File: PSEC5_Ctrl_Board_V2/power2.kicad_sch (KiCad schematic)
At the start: 41 parts, among them J1 1766343, U16 OKX-T/5-D12N-C, U5 OKX-T/5-D12N-C

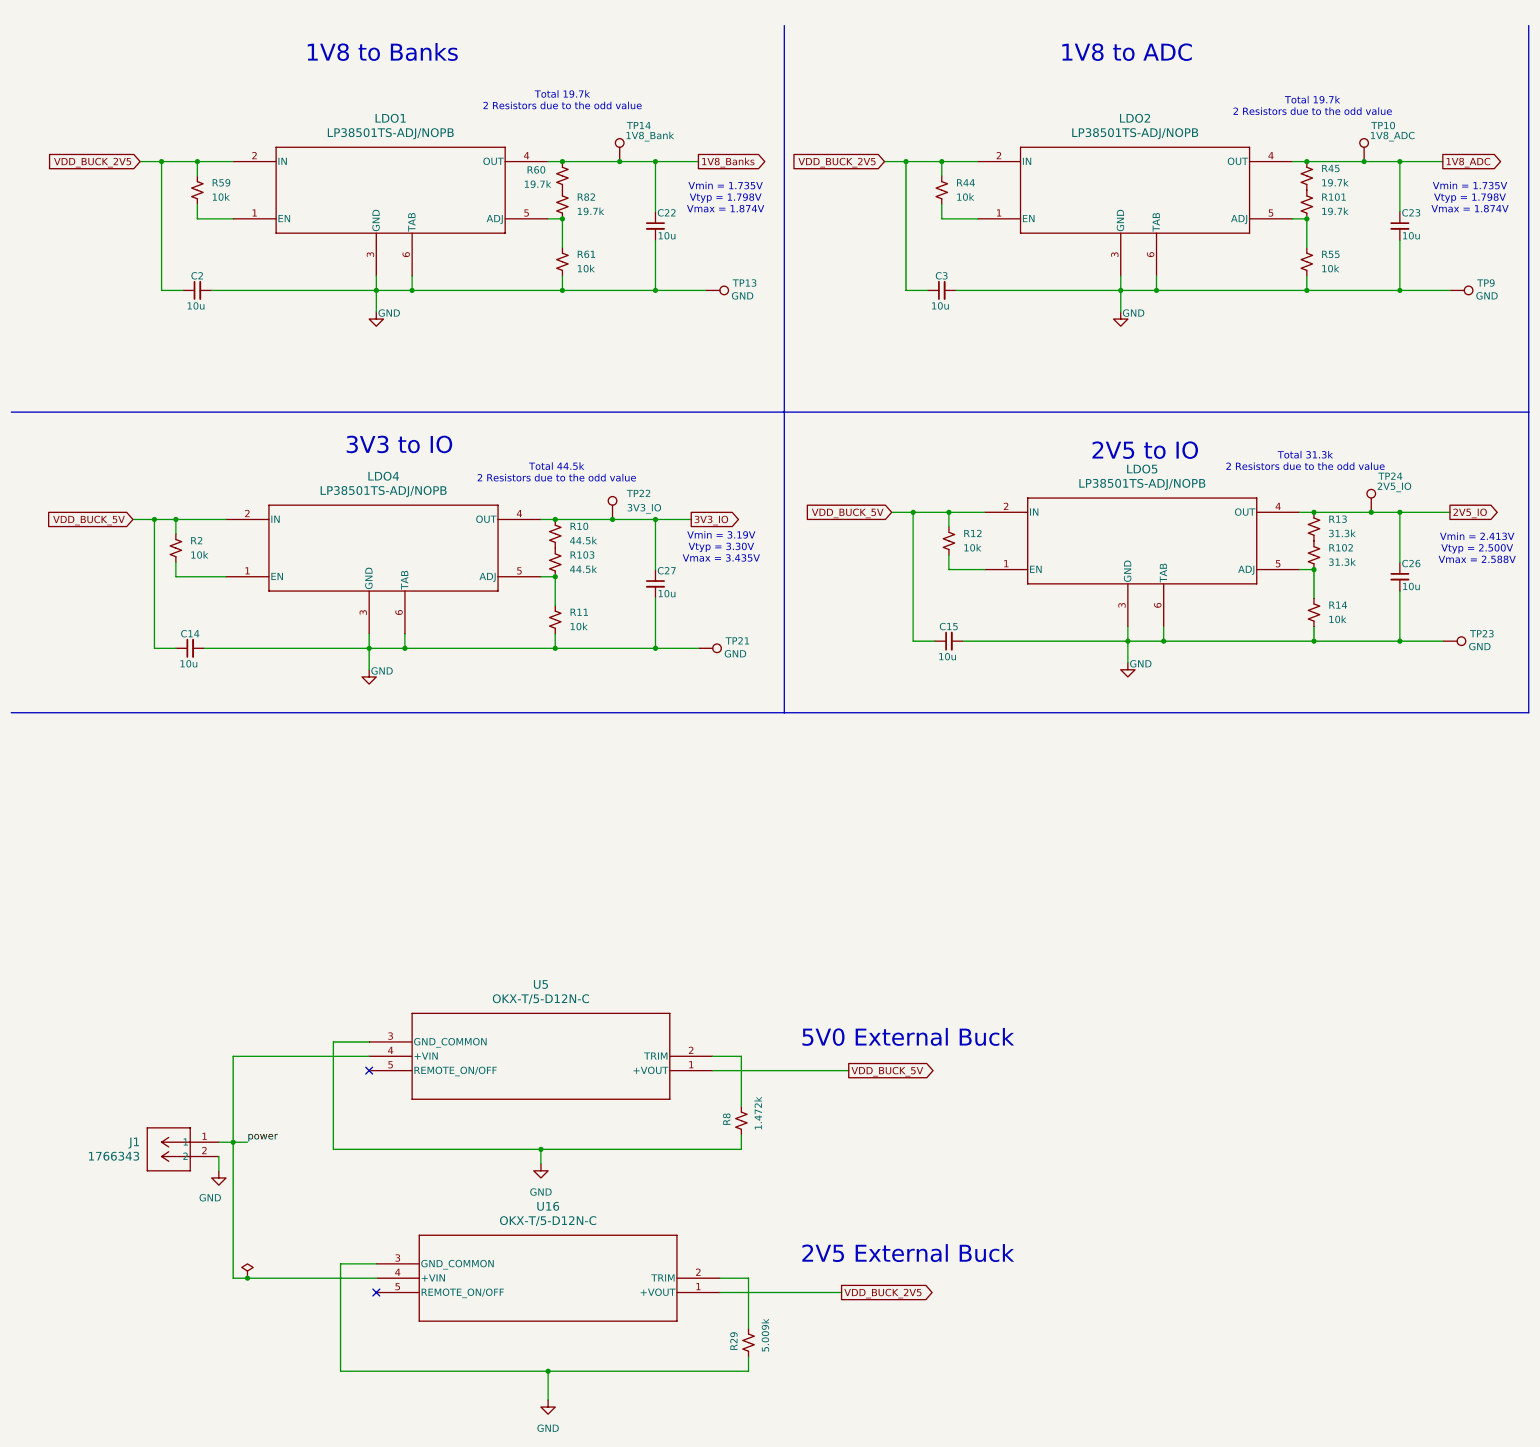
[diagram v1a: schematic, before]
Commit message: V2 Ready for Review
Everything added and new trace thickness + changes, Still need to add 5mm standoff pads, however I don't belive the measurements on the datasheet so I will review other parts first. Soldermask maybe needs some work too
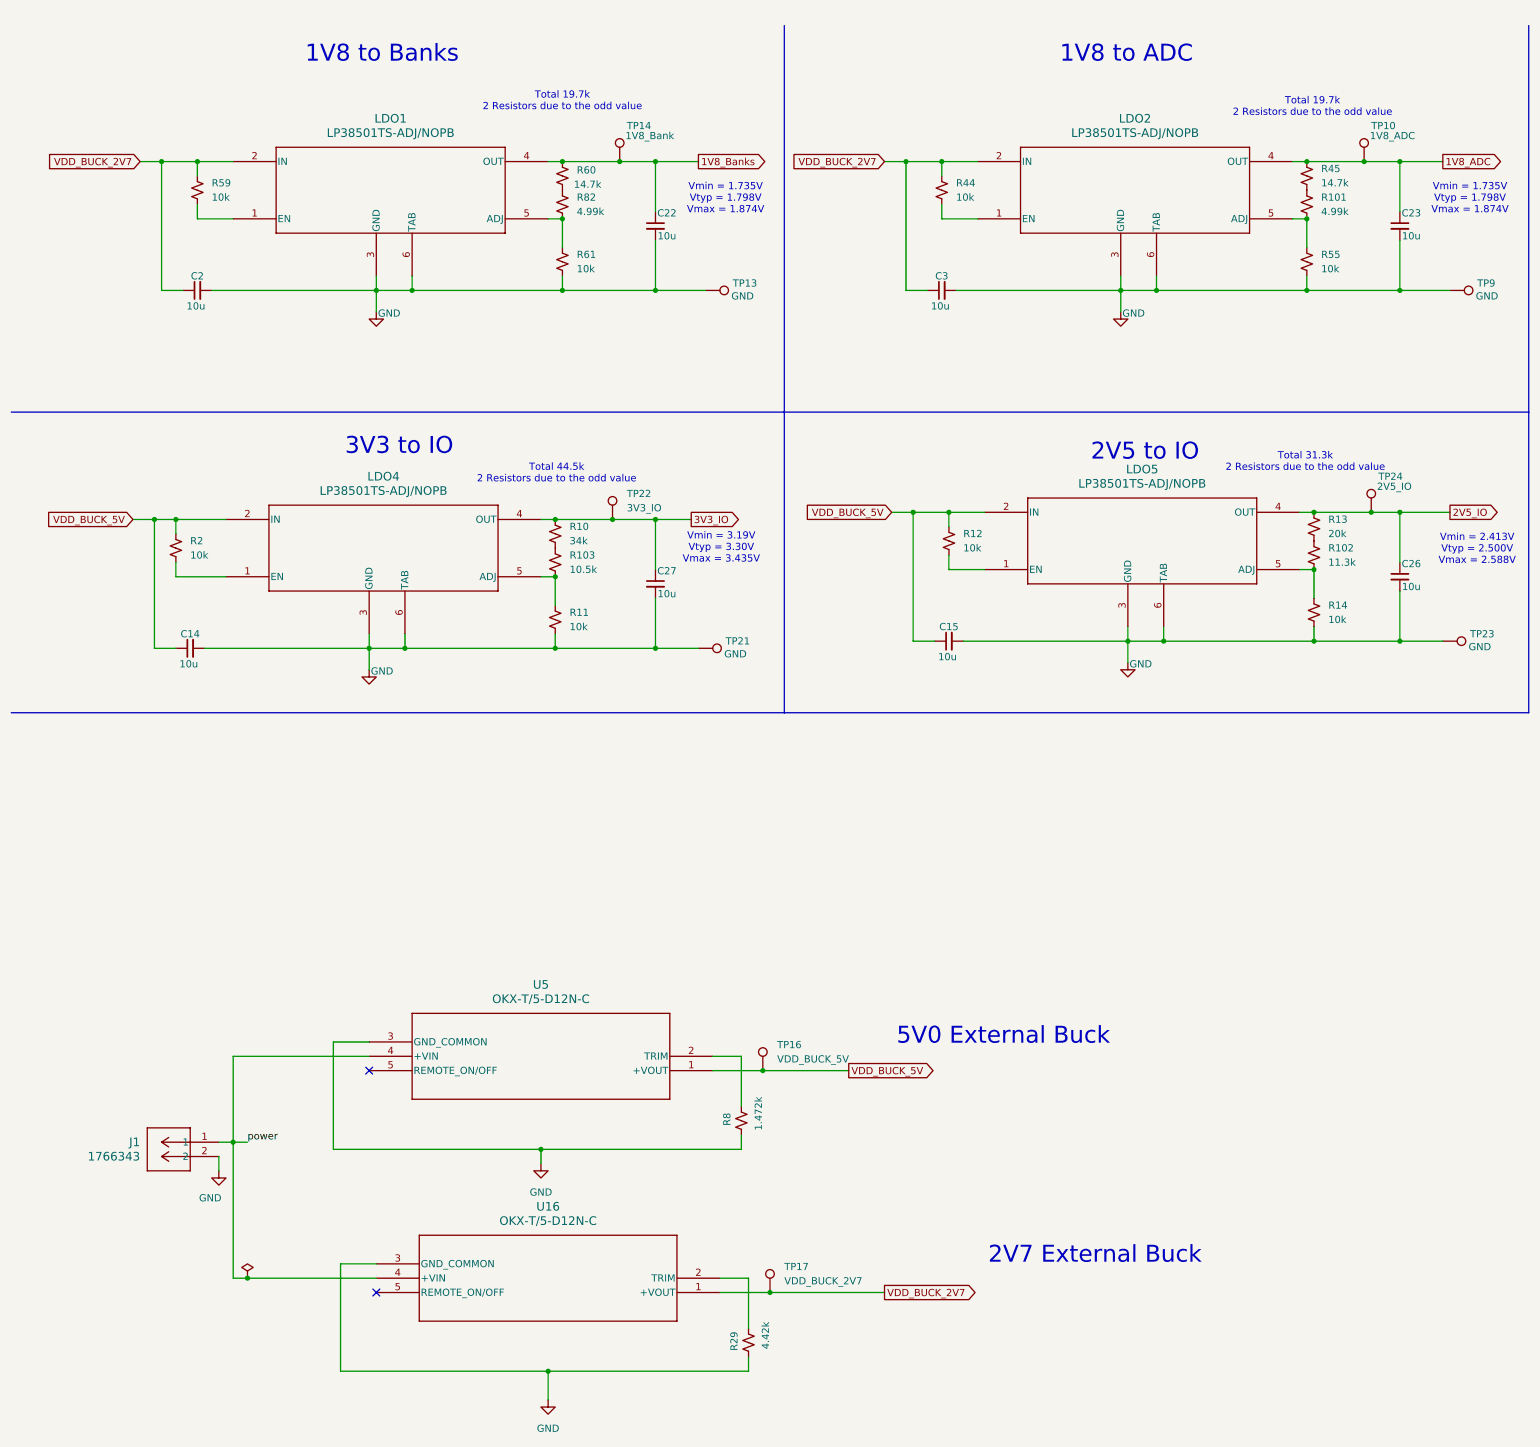
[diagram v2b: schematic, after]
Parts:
- added TP16: VDD_BUCK_5V, TestPoint:TestPoint_THTPad_1.5x1.5mm_Drill0.7mm, symbol Connector:TestPoint
- added TP17: VDD_BUCK_2V7, TestPoint:TestPoint_THTPad_1.5x1.5mm_Drill0.7mm, symbol Connector:TestPoint
- R10: value 44.5k -> 34k
- R101, R82: value 19.7k -> 4.99k
- R102: value 31.3k -> 11.3k
- R103: value 44.5k -> 10.5k
- R13: value 31.3k -> 20k
- R29: value 5.009k -> 4.42k
- R45, R60: value 19.7k -> 14.7k
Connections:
- net VDD_BUCK_5V: now also TP16.1
- net VDD_BUCK_2V5 renamed VDD_BUCK_2V7
- net VDD_BUCK_2V7: now also TP17.1
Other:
- note added: "2V7 External Buck"
- note removed: "2V5 External Buck"
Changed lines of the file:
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@@
 	(text "5V0 External Buck"
 		(exclude_from_sim no)
-		(at 171.704 192.532 0)
+		(at 188.722 192.024 0)
 		(effects
 			(font
@@
 		)
 	)
-	(text "2V5 External Buck"
+	(text "2V7 External Buck"
 		(exclude_from_sim no)
-		(at 171.704 230.886 0)
+		(at 204.978 230.886 0)
 		(effects
 			(font
@@
 	)
 	(junction
+		(at 147.32 237.49)
+		(diameter 0)
+		(color 0 0 0 0)
+	)
+	(junction
 		(at 120.65 36.83)
 		(diameter 0)
@@
 	)
 	(junction
+		(at 146.05 198.12)
+		(diameter 0)
+		(color 0 0 0 0)
+	)
+	(junction
 		(at 109.22 110.49)
 		(diameter 0)
@@
 	(wire
 		(pts
+			(xy 147.32 237.49) (xy 167.64 237.49)
+		)
+		(stroke
+			(width 0)
+			(type default)
+		)
+	)
+	(wire
+		(pts
 			(xy 259.08 36.83) (xy 266.7 36.83)
 		)
@@
 	(wire
 		(pts
+			(xy 146.05 198.12) (xy 161.29 198.12)
+		)
+		(stroke
+			(width 0)
+			(type default)
+		)
+	)
+	(wire
+		(pts
 			(xy 254 99.06) (xy 259.08 99.06)
 		)
@@
 	(wire
 		(pts
-			(xy 138.43 237.49) (xy 160.02 237.49)
+			(xy 138.43 237.49) (xy 147.32 237.49)
 		)
 		(stroke
@@
 	(wire
 		(pts
-			(xy 137.16 198.12) (xy 161.29 198.12)
+			(xy 137.16 198.12) (xy 146.05 198.12)
 		)
 		(stroke
@@
 		)
 	)
-	(global_label "VDD_BUCK_2V5"
+	(global_label "VDD_BUCK_2V7"
 		(shape input)
 		(at 35.56 36.83 180)
@@
 		)
 	)
-	(global_label "VDD_BUCK_2V5"
+	(global_label "VDD_BUCK_2V7"
 		(shape output)
-		(at 160.02 237.49 0)
+		(at 167.64 237.49 0)
 		(fields_autoplaced yes)
 		(effects
@@
 		)
 		(property "Intersheetrefs" "${INTERSHEET_REFS}"
-			(at 177.2171 237.49 0)
+			(at 184.8371 237.49 0)
 			(effects
 				(font
@@
 		)
 	)
-	(global_label "VDD_BUCK_2V5"
+	(global_label "VDD_BUCK_2V7"
 		(shape input)
 		(at 167.64 36.83 180)
@@
 			)
 		)
-		(property "Value" "44.5k"
+		(property "Value" "10.5k"
 			(at 111.76 109.2199 0)
 			(effects
@@
 	)
 	(symbol
+		(lib_id "Connector:TestPoint")
+		(at 146.05 198.12 0)
+		(unit 1)
+		(exclude_from_sim no)
+		(in_bom yes)
+		(on_board yes)
+		(dnp no)
+		(fields_autoplaced yes)
+		(property "Reference" "TP16"
+			(at 148.59 193.5479 0)
+			(effects
+				(font
+					(size 1.27 1.27)
+				)
+				(justify left)
+			)
+		)
+		(property "Value" "VDD_BUCK_5V"
+			(at 148.59 196.0879 0)
+			(effects
+				(font
+					(size 1.27 1.27)
+				)
+				(justify left)
+			)
+		)
+		(property "Footprint" "TestPoint:TestPoint_THTPad_1.5x1.5mm_Drill0.7mm"
+			(at 151.13 198.12 0)
+			(effects
+				(font
+					(size 1.27 1.27)
+				)
+				(hide yes)
+			)
+		)
+		(property "Datasheet" "~"
+			(at 151.13 198.12 0)
+			(effects
+				(font
+					(size 1.27 1.27)
+				)
+				(hide yes)
+			)
+		)
+		(property "Description" "test point"
+			(at 146.05 198.12 0)
+			(effects
+				(font
+					(size 1.27 1.27)
+				)
+				(hide yes)
+			)
+		)
+		(pin "1"
+		)
+		(instances
+			(project "PSEC5_Ctrl_Board"
+				(path "/165f2ae6-d522-4adf-a6c4-bb137b209d33/ba7b9281-d70b-432c-9c7d-bfda745e0250"
+					(reference "TP16")
+					(unit 1)
+				)
+			)
+		)
+	)
+	(symbol
 		(lib_id "Device:R_Small_US")
 		(at 242.57 54.61 0)
@@
 			)
 		)
-		(property "Value" "19.7k"
+		(property "Value" "4.99k"
 			(at 245.11 45.7199 0)
 			(effects
@@
 		(dnp no)
 		(property "Reference" "R60"
-			(at 104.14 38.354 0)
+			(at 113.03 38.354 0)
 			(effects
 				(font
@@
 			)
 		)
-		(property "Value" "19.7k"
-			(at 103.632 40.894 0)
+		(property "Value" "14.7k"
+			(at 112.522 40.894 0)
 			(effects
 				(font
@@
 			)
 		)
-		(property "Value" "31.3k"
+		(property "Value" "20k"
 			(at 246.38 102.8699 0)
 			(effects
@@
 			)
 		)
-		(property "Value" "19.7k"
+		(property "Value" "4.99k"
 			(at 113.03 45.7199 0)
 			(effects
@@
 			)
 		)
-		(property "Value" "19.7k"
+		(property "Value" "14.7k"
 			(at 245.11 40.6399 0)
 			(effects
@@
 			)
 		)
-		(property "Value" "5.009k"
+		(property "Value" "4.42k"
 			(at 146.558 245.11 90)
 			(effects
@@
 	)
 	(symbol
+		(lib_id "Connector:TestPoint")
+		(at 147.32 237.49 0)
+		(unit 1)
+		(exclude_from_sim no)
+		(in_bom yes)
+		(on_board yes)
+		(dnp no)
+		(fields_autoplaced yes)
+		(property "Reference" "TP17"
+			(at 149.86 232.9179 0)
+			(effects
+				(font
+					(size 1.27 1.27)
+				)
+				(justify left)
+			)
+		)
+		(property "Value" "VDD_BUCK_2V7"
+			(at 149.86 235.4579 0)
+			(effects
+				(font
+					(size 1.27 1.27)
+				)
+				(justify left)
+			)
+		)
+		(property "Footprint" "TestPoint:TestPoint_THTPad_1.5x1.5mm_Drill0.7mm"
+			(at 152.4 237.49 0)
+			(effects
+				(font
+					(size 1.27 1.27)
+				)
+				(hide yes)
+			)
+		)
+		(property "Datasheet" "~"
+			(at 152.4 237.49 0)
+			(effects
+				(font
+					(size 1.27 1.27)
+				)
+				(hide yes)
+			)
+		)
+		(property "Description" "test point"
+			(at 147.32 237.49 0)
+			(effects
+				(font
+					(size 1.27 1.27)
+				)
+				(hide yes)
+			)
+		)
+		(pin "1"
+		)
+		(instances
+			(project "PSEC5_Ctrl_Board"
+				(path "/165f2ae6-d522-4adf-a6c4-bb137b209d33/ba7b9281-d70b-432c-9c7d-bfda745e0250"
+					(reference "TP17")
+					(unit 1)
+				)
+			)
+		)
+	)
+	(symbol
 		(lib_id "power:GND")
 		(at 76.2 127 0)
@@
 			)
 		)
-		(property "Value" "44.5k"
+		(property "Value" "34k"
 			(at 111.76 104.1399 0)
 			(effects
@@
 			)
 		)
-		(property "Value" "31.3k"
+		(property "Value" "11.3k"
 			(at 246.38 107.9499 0)
 			(effects

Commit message: Made new File for final Controller
Created a new folder "KADC_CONTROLLER_V2" which is a copy of the control board v2 schematic to increase speed. Replaced with KADC CONTROLLER components and added signals for the new pins on PSEC6
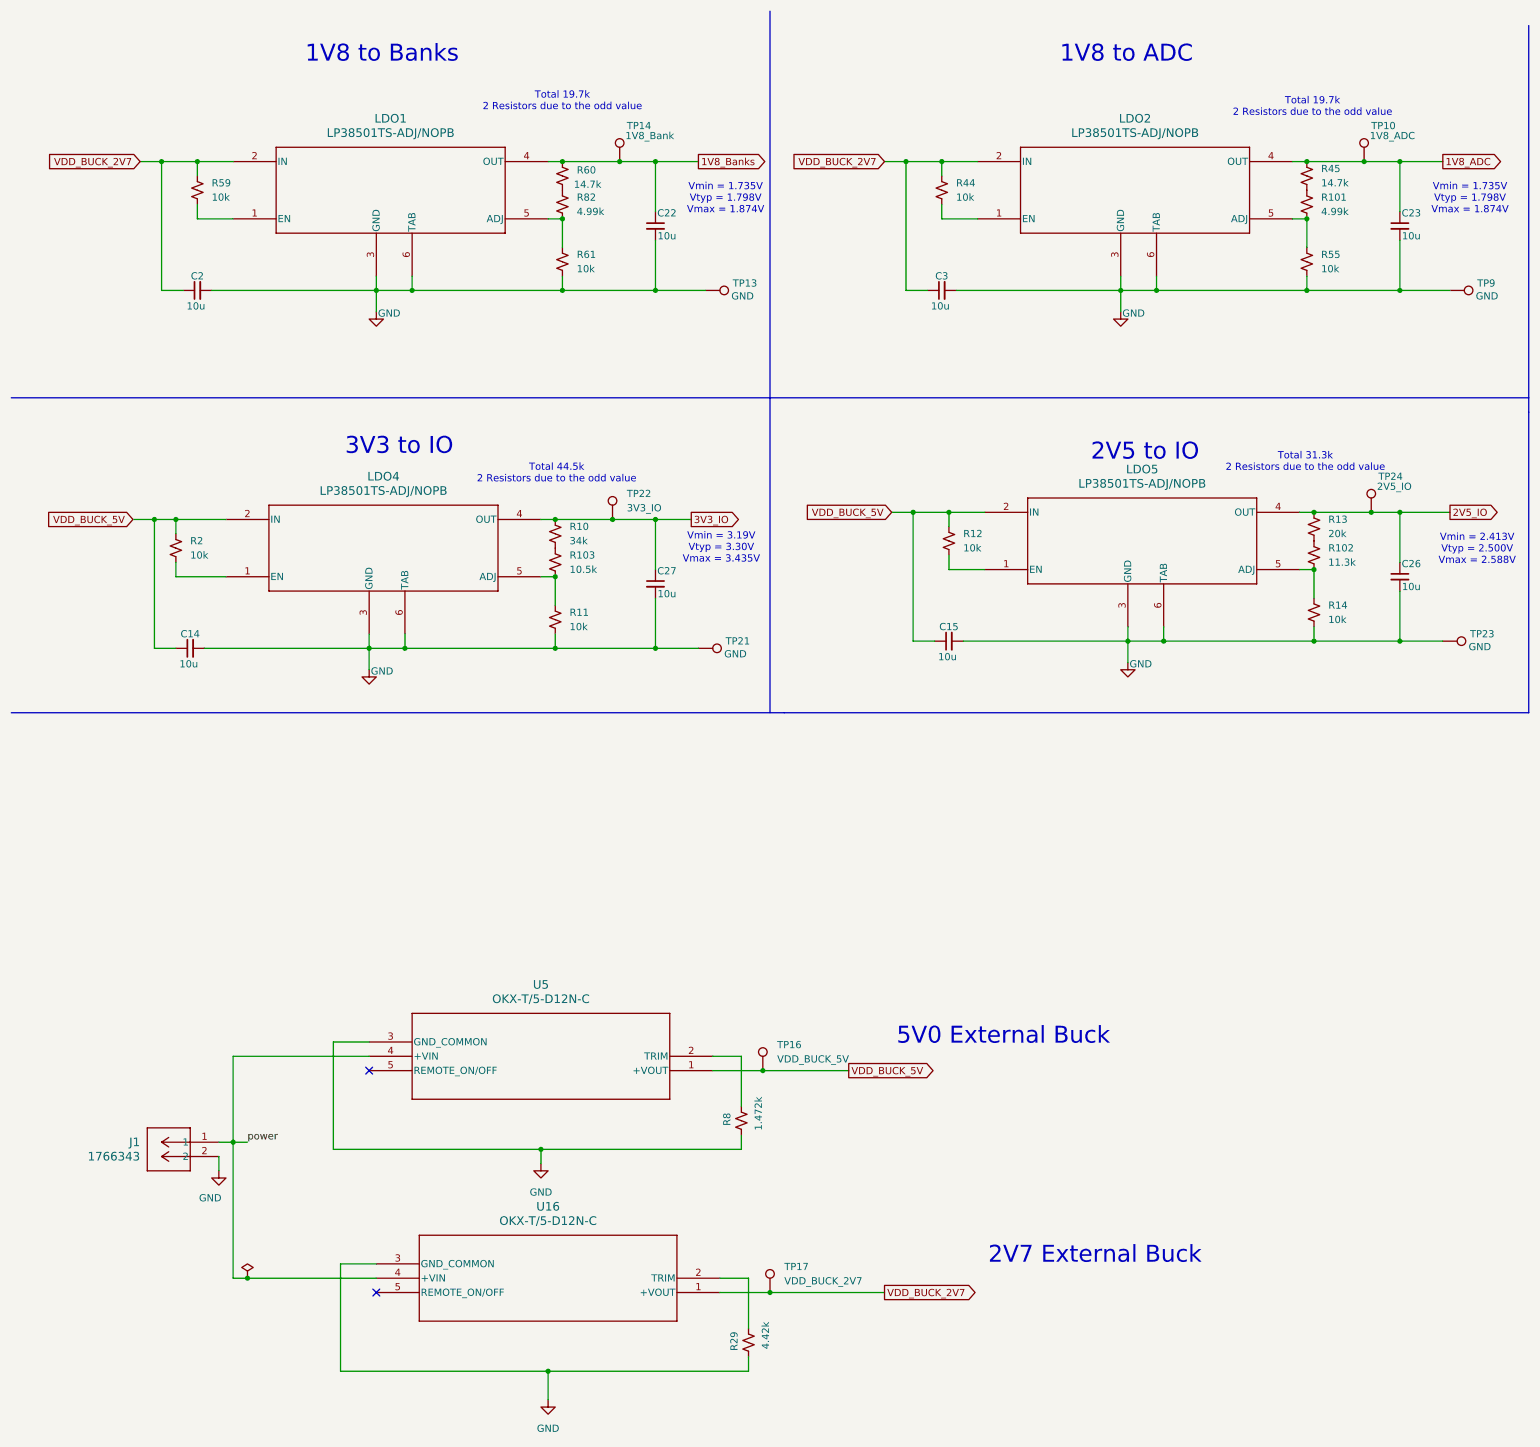
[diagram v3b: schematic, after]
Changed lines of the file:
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@@
 	(polyline
 		(pts
-			(xy 149.86 12.7) (xy 149.86 81.28)
+			(xy 147.32 10.16) (xy 147.32 78.74)
 		)
 		(stroke
@@
 	(polyline
 		(pts
-			(xy 12.7 81.28) (xy 149.86 81.28)
+			(xy 12.7 78.74) (xy 147.32 78.74)
 		)
 		(stroke
@@
 	(polyline
 		(pts
-			(xy 149.86 81.28) (xy 281.94 81.28)
+			(xy 147.32 78.74) (xy 281.94 78.74)
 		)
 		(stroke
@@
 	(polyline
 		(pts
-			(xy 149.86 81.28) (xy 149.86 134.62)
-		)
-		(stroke
+			(xy 147.32 78.74) (xy 147.32 134.62)
+		)
+		(stroke
